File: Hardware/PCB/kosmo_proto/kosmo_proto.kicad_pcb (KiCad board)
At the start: 2 copper layers, 100 x 55 mm, 567 parts, among them J1 Synth_power_2x5, J2 Conn_01x01, J3 Conn_01x01, J4 Conn_01x01, J5 Conn_01x01, J6 Conn_01x01, J7 Conn_01x01

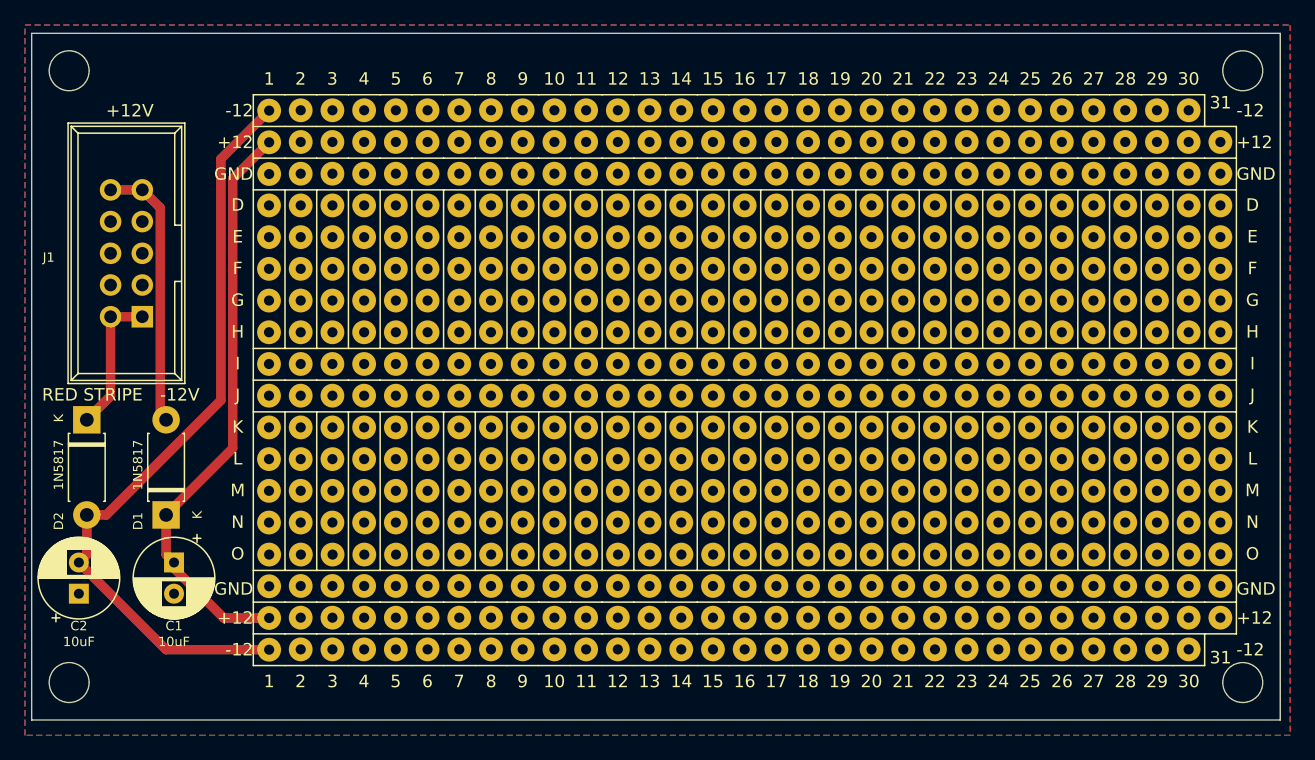
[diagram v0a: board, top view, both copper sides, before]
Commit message: Narrower version with jacks (kosmo_proto_j)
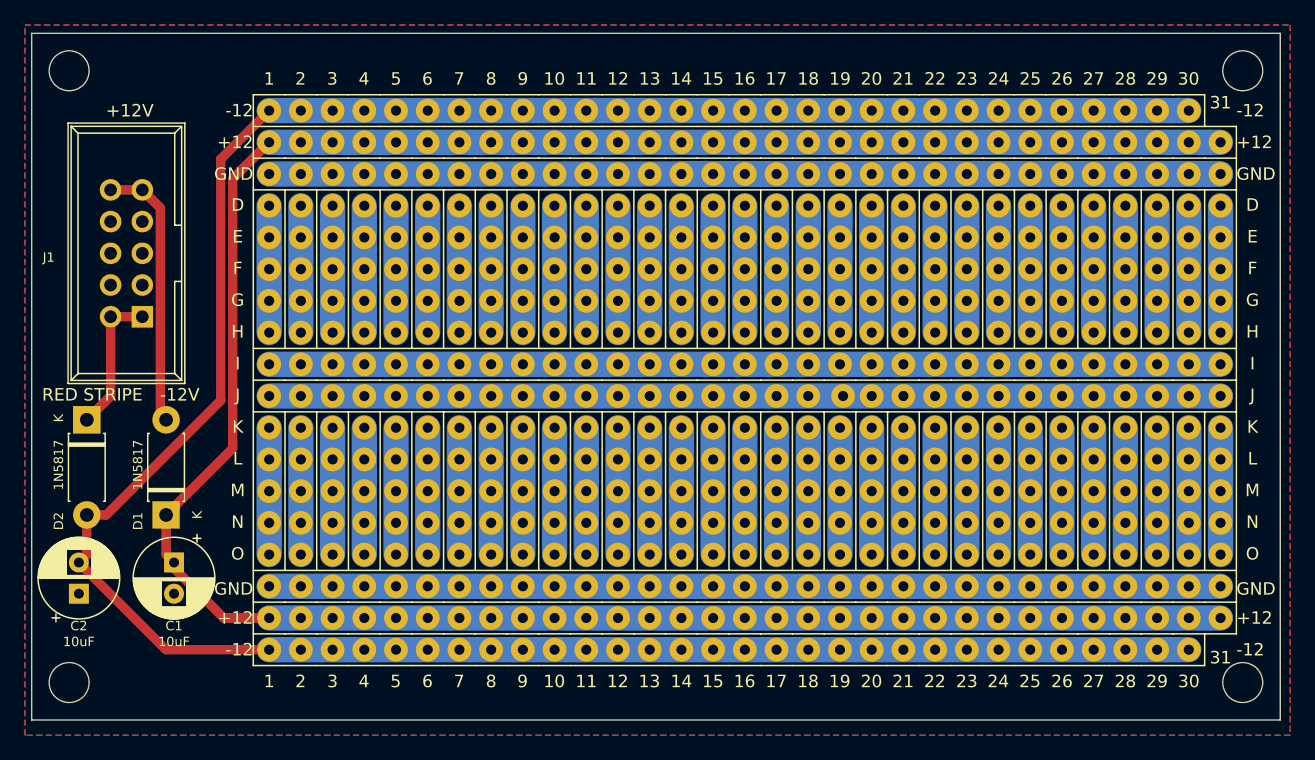
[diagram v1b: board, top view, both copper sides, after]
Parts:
- removed REF** (x4): MountingHole_3.2mm_M3, ao_tht:MountingHole_3.2mm_M3
- removed REF** (x550): PBH, ao_tht:Perf_Board_Hole
- added H1: MountingHole, ao_tht:MountingHole_3.2mm_M3, F.Cu at (48.8, 105.5)
- added H2: MountingHole, ao_tht:MountingHole_3.2mm_M3, F.Cu at (142.8, 105.5)
- added H3: MountingHole, ao_tht:MountingHole_3.2mm_M3, F.Cu at (48.8, 56.5)
- added H4: MountingHole, ao_tht:MountingHole_3.2mm_M3, F.Cu at (142.8, 56.5)
- added J10: 1x1, ao_tht:Perf_Board_Hole, F.Cu at (64.8, 80.0)
- added J100: 1x1, ao_tht:Perf_Board_Hole, F.Cu at (90.2, 80.0)
- added J101: 1x1, ao_tht:Perf_Board_Hole, F.Cu at (92.7, 59.7)
- added J102: 1x1, ao_tht:Perf_Board_Hole, F.Cu at (92.7, 62.2)
- added J103: 1x1, ao_tht:Perf_Board_Hole, F.Cu at (92.7, 64.8)
- added J104: 1x1, ao_tht:Perf_Board_Hole, F.Cu at (92.7, 67.3)
- added J105: 1x1, ao_tht:Perf_Board_Hole, F.Cu at (92.7, 69.8)
- added J106: 1x1, ao_tht:Perf_Board_Hole, F.Cu at (92.7, 72.4)
- added J107: 1x1, ao_tht:Perf_Board_Hole, F.Cu at (92.7, 74.9)
- added J108: 1x1, ao_tht:Perf_Board_Hole, F.Cu at (92.7, 77.5)
- added J109: 1x1, ao_tht:Perf_Board_Hole, F.Cu at (92.7, 80.0)
- added J11: 1x1, ao_tht:Perf_Board_Hole, F.Cu at (67.3, 59.7)
- added J110: 1x1, ao_tht:Perf_Board_Hole, F.Cu at (95.2, 59.7)
- added J111: 1x1, ao_tht:Perf_Board_Hole, F.Cu at (95.2, 62.2)
- added J112: 1x1, ao_tht:Perf_Board_Hole, F.Cu at (95.2, 64.8)
- added J113: 1x1, ao_tht:Perf_Board_Hole, F.Cu at (95.2, 67.3)
- added J114: 1x1, ao_tht:Perf_Board_Hole, F.Cu at (95.2, 69.8)
- added J115: 1x1, ao_tht:Perf_Board_Hole, F.Cu at (95.2, 72.4)
- added J116: 1x1, ao_tht:Perf_Board_Hole, F.Cu at (95.2, 74.9)
- added J117: 1x1, ao_tht:Perf_Board_Hole, F.Cu at (95.2, 77.5)
- added J118: 1x1, ao_tht:Perf_Board_Hole, F.Cu at (95.2, 80.0)
- added J119: 1x1, ao_tht:Perf_Board_Hole, F.Cu at (97.8, 59.7)
- added J12: 1x1, ao_tht:Perf_Board_Hole, F.Cu at (67.3, 62.2)
- added J120: 1x1, ao_tht:Perf_Board_Hole, F.Cu at (97.8, 62.2)
- added J121: 1x1, ao_tht:Perf_Board_Hole, F.Cu at (97.8, 64.8)
- added J122: 1x1, ao_tht:Perf_Board_Hole, F.Cu at (97.8, 67.3)
- added J123: 1x1, ao_tht:Perf_Board_Hole, F.Cu at (97.8, 69.8)
- added J124: 1x1, ao_tht:Perf_Board_Hole, F.Cu at (97.8, 72.4)
- added J125: 1x1, ao_tht:Perf_Board_Hole, F.Cu at (97.8, 74.9)
- added J126: 1x1, ao_tht:Perf_Board_Hole, F.Cu at (97.8, 77.5)
- added J127: 1x1, ao_tht:Perf_Board_Hole, F.Cu at (97.8, 80.0)
- added J128: 1x1, ao_tht:Perf_Board_Hole, F.Cu at (100.3, 59.7)
- added J129: 1x1, ao_tht:Perf_Board_Hole, F.Cu at (100.3, 62.2)
- added J13: 1x1, ao_tht:Perf_Board_Hole, F.Cu at (67.3, 64.8)
- added J130: 1x1, ao_tht:Perf_Board_Hole, F.Cu at (100.3, 64.8)
- added J131: 1x1, ao_tht:Perf_Board_Hole, F.Cu at (100.3, 67.3)
- added J132: 1x1, ao_tht:Perf_Board_Hole, F.Cu at (100.3, 69.8)
- added J133: 1x1, ao_tht:Perf_Board_Hole, F.Cu at (100.3, 72.4)
- added J134: 1x1, ao_tht:Perf_Board_Hole, F.Cu at (100.3, 74.9)
- added J135: 1x1, ao_tht:Perf_Board_Hole, F.Cu at (100.3, 77.5)
- added J136: 1x1, ao_tht:Perf_Board_Hole, F.Cu at (100.3, 80.0)
- added J137: 1x1, ao_tht:Perf_Board_Hole, F.Cu at (102.9, 59.7)
- added J138: 1x1, ao_tht:Perf_Board_Hole, F.Cu at (102.9, 62.2)
- added J139: 1x1, ao_tht:Perf_Board_Hole, F.Cu at (102.9, 64.8)
- added J14: 1x1, ao_tht:Perf_Board_Hole, F.Cu at (67.3, 67.3)
- added J140: 1x1, ao_tht:Perf_Board_Hole, F.Cu at (102.9, 67.3)
- added J141: 1x1, ao_tht:Perf_Board_Hole, F.Cu at (102.9, 69.8)
- added J142: 1x1, ao_tht:Perf_Board_Hole, F.Cu at (102.9, 72.4)
- added J143: 1x1, ao_tht:Perf_Board_Hole, F.Cu at (102.9, 74.9)
- added J144: 1x1, ao_tht:Perf_Board_Hole, F.Cu at (102.9, 77.5)
- added J145: 1x1, ao_tht:Perf_Board_Hole, F.Cu at (102.9, 80.0)
- added J146: 1x1, ao_tht:Perf_Board_Hole, F.Cu at (105.4, 59.7)
- added J147: 1x1, ao_tht:Perf_Board_Hole, F.Cu at (105.4, 62.2)
- added J148: 1x1, ao_tht:Perf_Board_Hole, F.Cu at (105.4, 64.8)
- added J149: 1x1, ao_tht:Perf_Board_Hole, F.Cu at (105.4, 67.3)
- added J15: 1x1, ao_tht:Perf_Board_Hole, F.Cu at (67.3, 69.8)
- added J150: 1x1, ao_tht:Perf_Board_Hole, F.Cu at (105.4, 69.8)
- added J151: 1x1, ao_tht:Perf_Board_Hole, F.Cu at (105.4, 72.4)
- added J152: 1x1, ao_tht:Perf_Board_Hole, F.Cu at (105.4, 74.9)
- added J153: 1x1, ao_tht:Perf_Board_Hole, F.Cu at (105.4, 77.5)
- added J154: 1x1, ao_tht:Perf_Board_Hole, F.Cu at (105.4, 80.0)
- added J155: 1x1, ao_tht:Perf_Board_Hole, F.Cu at (108.0, 59.7)
- added J156: 1x1, ao_tht:Perf_Board_Hole, F.Cu at (108.0, 62.2)
- added J157: 1x1, ao_tht:Perf_Board_Hole, F.Cu at (108.0, 64.8)
- added J158: 1x1, ao_tht:Perf_Board_Hole, F.Cu at (108.0, 67.3)
- added J159: 1x1, ao_tht:Perf_Board_Hole, F.Cu at (108.0, 69.8)
- added J16: 1x1, ao_tht:Perf_Board_Hole, F.Cu at (67.3, 72.4)
- added J160: 1x1, ao_tht:Perf_Board_Hole, F.Cu at (108.0, 72.4)
- added J161: 1x1, ao_tht:Perf_Board_Hole, F.Cu at (108.0, 74.9)
- added J162: 1x1, ao_tht:Perf_Board_Hole, F.Cu at (108.0, 77.5)
- added J163: 1x1, ao_tht:Perf_Board_Hole, F.Cu at (108.0, 80.0)
- added J164: 1x1, ao_tht:Perf_Board_Hole, F.Cu at (110.5, 59.7)
- added J165: 1x1, ao_tht:Perf_Board_Hole, F.Cu at (110.5, 62.2)
- added J166: 1x1, ao_tht:Perf_Board_Hole, F.Cu at (110.5, 64.8)
- added J167: 1x1, ao_tht:Perf_Board_Hole, F.Cu at (110.5, 67.3)
- added J168: 1x1, ao_tht:Perf_Board_Hole, F.Cu at (110.5, 69.8)
- added J169: 1x1, ao_tht:Perf_Board_Hole, F.Cu at (110.5, 72.4)
- added J17: 1x1, ao_tht:Perf_Board_Hole, F.Cu at (67.3, 74.9)
- added J170: 1x1, ao_tht:Perf_Board_Hole, F.Cu at (110.5, 74.9)
- added J171: 1x1, ao_tht:Perf_Board_Hole, F.Cu at (110.5, 77.5)
- added J172: 1x1, ao_tht:Perf_Board_Hole, F.Cu at (110.5, 80.0)
- added J173: 1x1, ao_tht:Perf_Board_Hole, F.Cu at (113.0, 59.7)
- added J174: 1x1, ao_tht:Perf_Board_Hole, F.Cu at (113.0, 62.2)
- added J175: 1x1, ao_tht:Perf_Board_Hole, F.Cu at (113.0, 64.8)
- added J176: 1x1, ao_tht:Perf_Board_Hole, F.Cu at (113.0, 67.3)
- added J177: 1x1, ao_tht:Perf_Board_Hole, F.Cu at (113.0, 69.8)
- added J178: 1x1, ao_tht:Perf_Board_Hole, F.Cu at (113.0, 72.4)
- added J179: 1x1, ao_tht:Perf_Board_Hole, F.Cu at (113.0, 74.9)
- added J18: 1x1, ao_tht:Perf_Board_Hole, F.Cu at (67.3, 77.5)
- added J180: 1x1, ao_tht:Perf_Board_Hole, F.Cu at (113.0, 77.5)
- added J181: 1x1, ao_tht:Perf_Board_Hole, F.Cu at (113.0, 80.0)
- added J182: 1x1, ao_tht:Perf_Board_Hole, F.Cu at (115.6, 59.7)
- added J183: 1x1, ao_tht:Perf_Board_Hole, F.Cu at (115.6, 62.2)
- added J184: 1x1, ao_tht:Perf_Board_Hole, F.Cu at (115.6, 64.8)
- added J185: 1x1, ao_tht:Perf_Board_Hole, F.Cu at (115.6, 67.3)
- added J186: 1x1, ao_tht:Perf_Board_Hole, F.Cu at (115.6, 69.8)
- added J187: 1x1, ao_tht:Perf_Board_Hole, F.Cu at (115.6, 72.4)
- added J188: 1x1, ao_tht:Perf_Board_Hole, F.Cu at (115.6, 74.9)
- added J189: 1x1, ao_tht:Perf_Board_Hole, F.Cu at (115.6, 77.5)
- added J19: 1x1, ao_tht:Perf_Board_Hole, F.Cu at (67.3, 80.0)
- added J190: 1x1, ao_tht:Perf_Board_Hole, F.Cu at (115.6, 80.0)
- added J191: 1x1, ao_tht:Perf_Board_Hole, F.Cu at (118.1, 59.7)
- added J192: 1x1, ao_tht:Perf_Board_Hole, F.Cu at (118.1, 62.2)
- added J193: 1x1, ao_tht:Perf_Board_Hole, F.Cu at (118.1, 64.8)
- added J194: 1x1, ao_tht:Perf_Board_Hole, F.Cu at (118.1, 67.3)
- added J195: 1x1, ao_tht:Perf_Board_Hole, F.Cu at (118.1, 69.8)
- added J196: 1x1, ao_tht:Perf_Board_Hole, F.Cu at (118.1, 72.4)
- added J197: 1x1, ao_tht:Perf_Board_Hole, F.Cu at (118.1, 74.9)
- added J198: 1x1, ao_tht:Perf_Board_Hole, F.Cu at (118.1, 77.5)
- added J199: 1x1, ao_tht:Perf_Board_Hole, F.Cu at (118.1, 80.0)
- added J20: 1x1, ao_tht:Perf_Board_Hole, F.Cu at (69.8, 59.7)
- added J200: 1x1, ao_tht:Perf_Board_Hole, F.Cu at (120.7, 59.7)
- added J201: 1x1, ao_tht:Perf_Board_Hole, F.Cu at (120.7, 62.2)
- added J202: 1x1, ao_tht:Perf_Board_Hole, F.Cu at (120.7, 64.8)
- added J203: 1x1, ao_tht:Perf_Board_Hole, F.Cu at (120.7, 67.3)
- added J204: 1x1, ao_tht:Perf_Board_Hole, F.Cu at (120.7, 69.8)
- added J205: 1x1, ao_tht:Perf_Board_Hole, F.Cu at (120.7, 72.4)
- added J206: 1x1, ao_tht:Perf_Board_Hole, F.Cu at (120.7, 74.9)
- added J207: 1x1, ao_tht:Perf_Board_Hole, F.Cu at (120.7, 77.5)
- added J208: 1x1, ao_tht:Perf_Board_Hole, F.Cu at (120.7, 80.0)
- added J209: 1x1, ao_tht:Perf_Board_Hole, F.Cu at (123.2, 59.7)
- added J21: 1x1, ao_tht:Perf_Board_Hole, F.Cu at (69.8, 62.2)
- added J210: 1x1, ao_tht:Perf_Board_Hole, F.Cu at (123.2, 62.2)
- added J211: 1x1, ao_tht:Perf_Board_Hole, F.Cu at (123.2, 64.8)
- added J212: 1x1, ao_tht:Perf_Board_Hole, F.Cu at (123.2, 67.3)
- added J213: 1x1, ao_tht:Perf_Board_Hole, F.Cu at (123.2, 69.8)
- added J214: 1x1, ao_tht:Perf_Board_Hole, F.Cu at (123.2, 72.4)
- added J215: 1x1, ao_tht:Perf_Board_Hole, F.Cu at (123.2, 74.9)
- added J216: 1x1, ao_tht:Perf_Board_Hole, F.Cu at (123.2, 77.5)
- added J217: 1x1, ao_tht:Perf_Board_Hole, F.Cu at (123.2, 80.0)
- added J218: 1x1, ao_tht:Perf_Board_Hole, F.Cu at (125.7, 59.7)
- added J219: 1x1, ao_tht:Perf_Board_Hole, F.Cu at (125.7, 62.2)
- added J22: 1x1, ao_tht:Perf_Board_Hole, F.Cu at (69.8, 64.8)
- added J220: 1x1, ao_tht:Perf_Board_Hole, F.Cu at (125.7, 64.8)
- added J221: 1x1, ao_tht:Perf_Board_Hole, F.Cu at (125.7, 67.3)
- added J222: 1x1, ao_tht:Perf_Board_Hole, F.Cu at (125.7, 69.8)
- added J223: 1x1, ao_tht:Perf_Board_Hole, F.Cu at (125.7, 72.4)
- added J224: 1x1, ao_tht:Perf_Board_Hole, F.Cu at (125.7, 74.9)
- added J225: 1x1, ao_tht:Perf_Board_Hole, F.Cu at (125.7, 77.5)
- added J226: 1x1, ao_tht:Perf_Board_Hole, F.Cu at (125.7, 80.0)
- added J227: 1x1, ao_tht:Perf_Board_Hole, F.Cu at (128.3, 59.7)
- added J228: 1x1, ao_tht:Perf_Board_Hole, F.Cu at (128.3, 62.2)
- added J229: 1x1, ao_tht:Perf_Board_Hole, F.Cu at (128.3, 64.8)
- added J23: 1x1, ao_tht:Perf_Board_Hole, F.Cu at (69.8, 67.3)
- added J230: 1x1, ao_tht:Perf_Board_Hole, F.Cu at (128.3, 67.3)
- added J231: 1x1, ao_tht:Perf_Board_Hole, F.Cu at (128.3, 69.8)
- added J232: 1x1, ao_tht:Perf_Board_Hole, F.Cu at (128.3, 72.4)
- added J233: 1x1, ao_tht:Perf_Board_Hole, F.Cu at (128.3, 74.9)
- added J234: 1x1, ao_tht:Perf_Board_Hole, F.Cu at (128.3, 77.5)
- added J235: 1x1, ao_tht:Perf_Board_Hole, F.Cu at (128.3, 80.0)
- added J236: 1x1, ao_tht:Perf_Board_Hole, F.Cu at (130.8, 59.7)
- added J237: 1x1, ao_tht:Perf_Board_Hole, F.Cu at (130.8, 62.2)
- added J238: 1x1, ao_tht:Perf_Board_Hole, F.Cu at (130.8, 64.8)
- added J239: 1x1, ao_tht:Perf_Board_Hole, F.Cu at (130.8, 67.3)
- added J24: 1x1, ao_tht:Perf_Board_Hole, F.Cu at (69.8, 69.8)
- added J240: 1x1, ao_tht:Perf_Board_Hole, F.Cu at (130.8, 69.8)
- added J241: 1x1, ao_tht:Perf_Board_Hole, F.Cu at (130.8, 72.4)
- added J242: 1x1, ao_tht:Perf_Board_Hole, F.Cu at (130.8, 74.9)
- added J243: 1x1, ao_tht:Perf_Board_Hole, F.Cu at (130.8, 77.5)
- added J244: 1x1, ao_tht:Perf_Board_Hole, F.Cu at (130.8, 80.0)
- added J245: 1x1, ao_tht:Perf_Board_Hole, F.Cu at (133.3, 59.7)
- added J246: 1x1, ao_tht:Perf_Board_Hole, F.Cu at (133.3, 62.2)
- added J247: 1x1, ao_tht:Perf_Board_Hole, F.Cu at (133.3, 64.8)
- added J248: 1x1, ao_tht:Perf_Board_Hole, F.Cu at (133.3, 67.3)
- added J249: 1x1, ao_tht:Perf_Board_Hole, F.Cu at (133.3, 69.8)
- added J25: 1x1, ao_tht:Perf_Board_Hole, F.Cu at (69.8, 72.4)
- added J250: 1x1, ao_tht:Perf_Board_Hole, F.Cu at (133.3, 72.4)
- added J251: 1x1, ao_tht:Perf_Board_Hole, F.Cu at (133.3, 74.9)
- added J252: 1x1, ao_tht:Perf_Board_Hole, F.Cu at (133.3, 77.5)
- added J253: 1x1, ao_tht:Perf_Board_Hole, F.Cu at (133.3, 80.0)
- added J254: 1x1, ao_tht:Perf_Board_Hole, F.Cu at (135.9, 59.7)
- added J255: 1x1, ao_tht:Perf_Board_Hole, F.Cu at (135.9, 62.2)
- added J256: 1x1, ao_tht:Perf_Board_Hole, F.Cu at (135.9, 64.8)
- added J257: 1x1, ao_tht:Perf_Board_Hole, F.Cu at (135.9, 67.3)
- added J258: 1x1, ao_tht:Perf_Board_Hole, F.Cu at (135.9, 69.8)
- added J259: 1x1, ao_tht:Perf_Board_Hole, F.Cu at (135.9, 72.4)
- added J26: 1x1, ao_tht:Perf_Board_Hole, F.Cu at (69.8, 74.9)
- added J260: 1x1, ao_tht:Perf_Board_Hole, F.Cu at (135.9, 74.9)
- added J261: 1x1, ao_tht:Perf_Board_Hole, F.Cu at (135.9, 77.5)
- added J262: 1x1, ao_tht:Perf_Board_Hole, F.Cu at (135.9, 80.0)
- added J263: 1x1, ao_tht:Perf_Board_Hole, F.Cu at (138.4, 59.7)
- added J264: 1x1, ao_tht:Perf_Board_Hole, F.Cu at (138.4, 62.2)
- added J265: 1x1, ao_tht:Perf_Board_Hole, F.Cu at (138.4, 64.8)
- added J266: 1x1, ao_tht:Perf_Board_Hole, F.Cu at (138.4, 67.3)
- added J267: 1x1, ao_tht:Perf_Board_Hole, F.Cu at (138.4, 69.8)
- added J268: 1x1, ao_tht:Perf_Board_Hole, F.Cu at (138.4, 72.4)
- added J269: 1x1, ao_tht:Perf_Board_Hole, F.Cu at (138.4, 74.9)
- added J27: 1x1, ao_tht:Perf_Board_Hole, F.Cu at (69.8, 77.5)
- added J270: 1x1, ao_tht:Perf_Board_Hole, F.Cu at (138.4, 77.5)
- added J271: 1x1, ao_tht:Perf_Board_Hole, F.Cu at (138.4, 80.0)
- added J273: 1x1, ao_tht:Perf_Board_Hole, F.Cu at (141.0, 62.2)
- added J274: 1x1, ao_tht:Perf_Board_Hole, F.Cu at (141.0, 64.8)
- added J275: 1x1, ao_tht:Perf_Board_Hole, F.Cu at (141.0, 67.3)
- added J276: 1x1, ao_tht:Perf_Board_Hole, F.Cu at (141.0, 69.8)
- added J277: 1x1, ao_tht:Perf_Board_Hole, F.Cu at (141.0, 72.4)
- added J278: 1x1, ao_tht:Perf_Board_Hole, F.Cu at (141.0, 74.9)
- added J279: 1x1, ao_tht:Perf_Board_Hole, F.Cu at (141.0, 77.5)
- added J28: 1x1, ao_tht:Perf_Board_Hole, F.Cu at (69.8, 80.0)
- added J280: 1x1, ao_tht:Perf_Board_Hole, F.Cu at (141.0, 80.0)
- added J281: 1x1, ao_tht:Perf_Board_Hole, F.Cu at (64.8, 82.5)
- added J282: 1x1, ao_tht:Perf_Board_Hole, F.Cu at (64.8, 85.1)
- added J283: 1x1, ao_tht:Perf_Board_Hole, F.Cu at (64.8, 87.6)
- added J284: 1x1, ao_tht:Perf_Board_Hole, F.Cu at (64.8, 90.2)
- added J285: 1x1, ao_tht:Perf_Board_Hole, F.Cu at (64.8, 92.7)
- added J286: 1x1, ao_tht:Perf_Board_Hole, F.Cu at (64.8, 95.2)
- added J287: 1x1, ao_tht:Perf_Board_Hole, F.Cu at (64.8, 97.8)
- added J288: 1x1, ao_tht:Perf_Board_Hole, F.Cu at (64.8, 100.3)
- added J289: 1x1, ao_tht:Perf_Board_Hole, F.Cu at (64.8, 102.9)
- added J29: 1x1, ao_tht:Perf_Board_Hole, F.Cu at (72.4, 59.7)
- added J290: 1x1, ao_tht:Perf_Board_Hole, F.Cu at (67.3, 82.5)
- added J291: 1x1, ao_tht:Perf_Board_Hole, F.Cu at (67.3, 85.1)
- added J292: 1x1, ao_tht:Perf_Board_Hole, F.Cu at (67.3, 87.6)
- added J293: 1x1, ao_tht:Perf_Board_Hole, F.Cu at (67.3, 90.2)
- added J294: 1x1, ao_tht:Perf_Board_Hole, F.Cu at (67.3, 92.7)
- added J295: 1x1, ao_tht:Perf_Board_Hole, F.Cu at (67.3, 95.2)
- added J296: 1x1, ao_tht:Perf_Board_Hole, F.Cu at (67.3, 97.8)
- added J297: 1x1, ao_tht:Perf_Board_Hole, F.Cu at (67.3, 100.3)
- added J298: 1x1, ao_tht:Perf_Board_Hole, F.Cu at (67.3, 102.9)
- added J299: 1x1, ao_tht:Perf_Board_Hole, F.Cu at (69.8, 82.5)
- added J30: 1x1, ao_tht:Perf_Board_Hole, F.Cu at (72.4, 62.2)
- added J300: 1x1, ao_tht:Perf_Board_Hole, F.Cu at (69.8, 85.1)
- added J301: 1x1, ao_tht:Perf_Board_Hole, F.Cu at (69.8, 87.6)
- added J302: 1x1, ao_tht:Perf_Board_Hole, F.Cu at (69.8, 90.2)
- added J303: 1x1, ao_tht:Perf_Board_Hole, F.Cu at (69.8, 92.7)
- added J304: 1x1, ao_tht:Perf_Board_Hole, F.Cu at (69.8, 95.2)
- added J305: 1x1, ao_tht:Perf_Board_Hole, F.Cu at (69.8, 97.8)
- added J306: 1x1, ao_tht:Perf_Board_Hole, F.Cu at (69.8, 100.3)
- added J307: 1x1, ao_tht:Perf_Board_Hole, F.Cu at (69.8, 102.9)
- added J308: 1x1, ao_tht:Perf_Board_Hole, F.Cu at (72.4, 82.5)
- added J309: 1x1, ao_tht:Perf_Board_Hole, F.Cu at (72.4, 85.1)
- added J31: 1x1, ao_tht:Perf_Board_Hole, F.Cu at (72.4, 64.8)
- added J310: 1x1, ao_tht:Perf_Board_Hole, F.Cu at (72.4, 87.6)
- added J311: 1x1, ao_tht:Perf_Board_Hole, F.Cu at (72.4, 90.2)
- added J312: 1x1, ao_tht:Perf_Board_Hole, F.Cu at (72.4, 92.7)
- added J313: 1x1, ao_tht:Perf_Board_Hole, F.Cu at (72.4, 95.2)
- added J314: 1x1, ao_tht:Perf_Board_Hole, F.Cu at (72.4, 97.8)
- added J315: 1x1, ao_tht:Perf_Board_Hole, F.Cu at (72.4, 100.3)
- added J316: 1x1, ao_tht:Perf_Board_Hole, F.Cu at (72.4, 102.9)
- added J317: 1x1, ao_tht:Perf_Board_Hole, F.Cu at (74.9, 82.5)
- added J318: 1x1, ao_tht:Perf_Board_Hole, F.Cu at (74.9, 85.1)
- added J319: 1x1, ao_tht:Perf_Board_Hole, F.Cu at (74.9, 87.6)
- added J32: 1x1, ao_tht:Perf_Board_Hole, F.Cu at (72.4, 67.3)
- added J320: 1x1, ao_tht:Perf_Board_Hole, F.Cu at (74.9, 90.2)
- added J321: 1x1, ao_tht:Perf_Board_Hole, F.Cu at (74.9, 92.7)
- added J322: 1x1, ao_tht:Perf_Board_Hole, F.Cu at (74.9, 95.2)
- added J323: 1x1, ao_tht:Perf_Board_Hole, F.Cu at (74.9, 97.8)
- added J324: 1x1, ao_tht:Perf_Board_Hole, F.Cu at (74.9, 100.3)
- added J325: 1x1, ao_tht:Perf_Board_Hole, F.Cu at (74.9, 102.9)
- added J326: 1x1, ao_tht:Perf_Board_Hole, F.Cu at (77.5, 82.5)
- added J327: 1x1, ao_tht:Perf_Board_Hole, F.Cu at (77.5, 85.1)
- added J328: 1x1, ao_tht:Perf_Board_Hole, F.Cu at (77.5, 87.6)
- added J329: 1x1, ao_tht:Perf_Board_Hole, F.Cu at (77.5, 90.2)
- added J33: 1x1, ao_tht:Perf_Board_Hole, F.Cu at (72.4, 69.8)
- added J330: 1x1, ao_tht:Perf_Board_Hole, F.Cu at (77.5, 92.7)
- added J331: 1x1, ao_tht:Perf_Board_Hole, F.Cu at (77.5, 95.2)
- added J332: 1x1, ao_tht:Perf_Board_Hole, F.Cu at (77.5, 97.8)
- added J333: 1x1, ao_tht:Perf_Board_Hole, F.Cu at (77.5, 100.3)
- added J334: 1x1, ao_tht:Perf_Board_Hole, F.Cu at (77.5, 102.9)
- added J335: 1x1, ao_tht:Perf_Board_Hole, F.Cu at (80.0, 82.5)
- added J336: 1x1, ao_tht:Perf_Board_Hole, F.Cu at (80.0, 85.1)
- added J337: 1x1, ao_tht:Perf_Board_Hole, F.Cu at (80.0, 87.6)
- added J338: 1x1, ao_tht:Perf_Board_Hole, F.Cu at (80.0, 90.2)
- added J339: 1x1, ao_tht:Perf_Board_Hole, F.Cu at (80.0, 92.7)
- added J34: 1x1, ao_tht:Perf_Board_Hole, F.Cu at (72.4, 72.4)
- added J340: 1x1, ao_tht:Perf_Board_Hole, F.Cu at (80.0, 95.2)
- added J341: 1x1, ao_tht:Perf_Board_Hole, F.Cu at (80.0, 97.8)
- added J342: 1x1, ao_tht:Perf_Board_Hole, F.Cu at (80.0, 100.3)
- added J343: 1x1, ao_tht:Perf_Board_Hole, F.Cu at (80.0, 102.9)
- added J344: 1x1, ao_tht:Perf_Board_Hole, F.Cu at (82.5, 82.5)
- added J345: 1x1, ao_tht:Perf_Board_Hole, F.Cu at (82.5, 85.1)
- added J346: 1x1, ao_tht:Perf_Board_Hole, F.Cu at (82.5, 87.6)
- added J347: 1x1, ao_tht:Perf_Board_Hole, F.Cu at (82.5, 90.2)
- added J348: 1x1, ao_tht:Perf_Board_Hole, F.Cu at (82.5, 92.7)
- added J349: 1x1, ao_tht:Perf_Board_Hole, F.Cu at (82.5, 95.2)
- added J35: 1x1, ao_tht:Perf_Board_Hole, F.Cu at (72.4, 74.9)
- added J350: 1x1, ao_tht:Perf_Board_Hole, F.Cu at (82.5, 97.8)
- added J351: 1x1, ao_tht:Perf_Board_Hole, F.Cu at (82.5, 100.3)
- added J352: 1x1, ao_tht:Perf_Board_Hole, F.Cu at (82.5, 102.9)
- added J353: 1x1, ao_tht:Perf_Board_Hole, F.Cu at (85.1, 82.5)
- added J354: 1x1, ao_tht:Perf_Board_Hole, F.Cu at (85.1, 85.1)
- added J355: 1x1, ao_tht:Perf_Board_Hole, F.Cu at (85.1, 87.6)
- added J356: 1x1, ao_tht:Perf_Board_Hole, F.Cu at (85.1, 90.2)
- added J357: 1x1, ao_tht:Perf_Board_Hole, F.Cu at (85.1, 92.7)
- added J358: 1x1, ao_tht:Perf_Board_Hole, F.Cu at (85.1, 95.2)
- added J359: 1x1, ao_tht:Perf_Board_Hole, F.Cu at (85.1, 97.8)
- added J36: 1x1, ao_tht:Perf_Board_Hole, F.Cu at (72.4, 77.5)
- added J360: 1x1, ao_tht:Perf_Board_Hole, F.Cu at (85.1, 100.3)
- added J361: 1x1, ao_tht:Perf_Board_Hole, F.Cu at (85.1, 102.9)
- added J362: 1x1, ao_tht:Perf_Board_Hole, F.Cu at (87.6, 82.5)
- added J363: 1x1, ao_tht:Perf_Board_Hole, F.Cu at (87.6, 85.1)
- added J364: 1x1, ao_tht:Perf_Board_Hole, F.Cu at (87.6, 87.6)
- added J365: 1x1, ao_tht:Perf_Board_Hole, F.Cu at (87.6, 90.2)
- added J366: 1x1, ao_tht:Perf_Board_Hole, F.Cu at (87.6, 92.7)
- added J367: 1x1, ao_tht:Perf_Board_Hole, F.Cu at (87.6, 95.2)
- added J368: 1x1, ao_tht:Perf_Board_Hole, F.Cu at (87.6, 97.8)
- added J369: 1x1, ao_tht:Perf_Board_Hole, F.Cu at (87.6, 100.3)
- added J37: 1x1, ao_tht:Perf_Board_Hole, F.Cu at (72.4, 80.0)
- added J370: 1x1, ao_tht:Perf_Board_Hole, F.Cu at (87.6, 102.9)
- added J371: 1x1, ao_tht:Perf_Board_Hole, F.Cu at (90.2, 82.5)
- added J372: 1x1, ao_tht:Perf_Board_Hole, F.Cu at (90.2, 85.1)
- added J373: 1x1, ao_tht:Perf_Board_Hole, F.Cu at (90.2, 87.6)
- added J374: 1x1, ao_tht:Perf_Board_Hole, F.Cu at (90.2, 90.2)
- added J375: 1x1, ao_tht:Perf_Board_Hole, F.Cu at (90.2, 92.7)
- added J376: 1x1, ao_tht:Perf_Board_Hole, F.Cu at (90.2, 95.2)
- added J377: 1x1, ao_tht:Perf_Board_Hole, F.Cu at (90.2, 97.8)
- added J378: 1x1, ao_tht:Perf_Board_Hole, F.Cu at (90.2, 100.3)
- added J379: 1x1, ao_tht:Perf_Board_Hole, F.Cu at (90.2, 102.9)
- added J38: 1x1, ao_tht:Perf_Board_Hole, F.Cu at (74.9, 59.7)
- added J380: 1x1, ao_tht:Perf_Board_Hole, F.Cu at (92.7, 82.5)
- added J381: 1x1, ao_tht:Perf_Board_Hole, F.Cu at (92.7, 85.1)
- added J382: 1x1, ao_tht:Perf_Board_Hole, F.Cu at (92.7, 87.6)
- added J383: 1x1, ao_tht:Perf_Board_Hole, F.Cu at (92.7, 90.2)
- added J384: 1x1, ao_tht:Perf_Board_Hole, F.Cu at (92.7, 92.7)
- added J385: 1x1, ao_tht:Perf_Board_Hole, F.Cu at (92.7, 95.2)
- added J386: 1x1, ao_tht:Perf_Board_Hole, F.Cu at (92.7, 97.8)
- added J387: 1x1, ao_tht:Perf_Board_Hole, F.Cu at (92.7, 100.3)
- added J388: 1x1, ao_tht:Perf_Board_Hole, F.Cu at (92.7, 102.9)
- added J389: 1x1, ao_tht:Perf_Board_Hole, F.Cu at (95.2, 82.5)
- added J39: 1x1, ao_tht:Perf_Board_Hole, F.Cu at (74.9, 62.2)
- added J390: 1x1, ao_tht:Perf_Board_Hole, F.Cu at (95.2, 85.1)
- added J391: 1x1, ao_tht:Perf_Board_Hole, F.Cu at (95.2, 87.6)
- added J392: 1x1, ao_tht:Perf_Board_Hole, F.Cu at (95.2, 90.2)
- added J393: 1x1, ao_tht:Perf_Board_Hole, F.Cu at (95.2, 92.7)
- added J394: 1x1, ao_tht:Perf_Board_Hole, F.Cu at (95.2, 95.2)
- added J395: 1x1, ao_tht:Perf_Board_Hole, F.Cu at (95.2, 97.8)
- added J396: 1x1, ao_tht:Perf_Board_Hole, F.Cu at (95.2, 100.3)
- added J397: 1x1, ao_tht:Perf_Board_Hole, F.Cu at (95.2, 102.9)
- added J398: 1x1, ao_tht:Perf_Board_Hole, F.Cu at (97.8, 82.5)
- added J399: 1x1, ao_tht:Perf_Board_Hole, F.Cu at (97.8, 85.1)
- added J40: 1x1, ao_tht:Perf_Board_Hole, F.Cu at (74.9, 64.8)
- added J400: 1x1, ao_tht:Perf_Board_Hole, F.Cu at (97.8, 87.6)
- added J401: 1x1, ao_tht:Perf_Board_Hole, F.Cu at (97.8, 90.2)
- added J402: 1x1, ao_tht:Perf_Board_Hole, F.Cu at (97.8, 92.7)
- added J403: 1x1, ao_tht:Perf_Board_Hole, F.Cu at (97.8, 95.2)
- added J404: 1x1, ao_tht:Perf_Board_Hole, F.Cu at (97.8, 97.8)
- added J405: 1x1, ao_tht:Perf_Board_Hole, F.Cu at (97.8, 100.3)
- added J406: 1x1, ao_tht:Perf_Board_Hole, F.Cu at (97.8, 102.9)
- added J407: 1x1, ao_tht:Perf_Board_Hole, F.Cu at (100.3, 82.5)
- added J408: 1x1, ao_tht:Perf_Board_Hole, F.Cu at (100.3, 85.1)
- added J409: 1x1, ao_tht:Perf_Board_Hole, F.Cu at (100.3, 87.6)
- added J41: 1x1, ao_tht:Perf_Board_Hole, F.Cu at (74.9, 67.3)
- added J410: 1x1, ao_tht:Perf_Board_Hole, F.Cu at (100.3, 90.2)
- added J411: 1x1, ao_tht:Perf_Board_Hole, F.Cu at (100.3, 92.7)
- added J412: 1x1, ao_tht:Perf_Board_Hole, F.Cu at (100.3, 95.2)
- added J413: 1x1, ao_tht:Perf_Board_Hole, F.Cu at (100.3, 97.8)
- added J414: 1x1, ao_tht:Perf_Board_Hole, F.Cu at (100.3, 100.3)
- added J415: 1x1, ao_tht:Perf_Board_Hole, F.Cu at (100.3, 102.9)
- added J416: 1x1, ao_tht:Perf_Board_Hole, F.Cu at (102.9, 82.5)
- added J417: 1x1, ao_tht:Perf_Board_Hole, F.Cu at (102.9, 85.1)
- added J418: 1x1, ao_tht:Perf_Board_Hole, F.Cu at (102.9, 87.6)
- added J419: 1x1, ao_tht:Perf_Board_Hole, F.Cu at (102.9, 90.2)
- added J42: 1x1, ao_tht:Perf_Board_Hole, F.Cu at (74.9, 69.8)
- added J420: 1x1, ao_tht:Perf_Board_Hole, F.Cu at (102.9, 92.7)
- added J421: 1x1, ao_tht:Perf_Board_Hole, F.Cu at (102.9, 95.2)
- added J422: 1x1, ao_tht:Perf_Board_Hole, F.Cu at (102.9, 97.8)
- added J423: 1x1, ao_tht:Perf_Board_Hole, F.Cu at (102.9, 100.3)
- added J424: 1x1, ao_tht:Perf_Board_Hole, F.Cu at (102.9, 102.9)
- added J425: 1x1, ao_tht:Perf_Board_Hole, F.Cu at (105.4, 82.5)
- added J426: 1x1, ao_tht:Perf_Board_Hole, F.Cu at (105.4, 85.1)
- added J427: 1x1, ao_tht:Perf_Board_Hole, F.Cu at (105.4, 87.6)
- added J428: 1x1, ao_tht:Perf_Board_Hole, F.Cu at (105.4, 90.2)
- added J429: 1x1, ao_tht:Perf_Board_Hole, F.Cu at (105.4, 92.7)
- added J43: 1x1, ao_tht:Perf_Board_Hole, F.Cu at (74.9, 72.4)
- added J430: 1x1, ao_tht:Perf_Board_Hole, F.Cu at (105.4, 95.2)
- added J431: 1x1, ao_tht:Perf_Board_Hole, F.Cu at (105.4, 97.8)
- added J432: 1x1, ao_tht:Perf_Board_Hole, F.Cu at (105.4, 100.3)
- added J433: 1x1, ao_tht:Perf_Board_Hole, F.Cu at (105.4, 102.9)
- added J434: 1x1, ao_tht:Perf_Board_Hole, F.Cu at (108.0, 82.5)
- added J435: 1x1, ao_tht:Perf_Board_Hole, F.Cu at (108.0, 85.1)
- added J436: 1x1, ao_tht:Perf_Board_Hole, F.Cu at (108.0, 87.6)
- added J437: 1x1, ao_tht:Perf_Board_Hole, F.Cu at (108.0, 90.2)
- added J438: 1x1, ao_tht:Perf_Board_Hole, F.Cu at (108.0, 92.7)
- added J439: 1x1, ao_tht:Perf_Board_Hole, F.Cu at (108.0, 95.2)
- added J44: 1x1, ao_tht:Perf_Board_Hole, F.Cu at (74.9, 74.9)
- added J440: 1x1, ao_tht:Perf_Board_Hole, F.Cu at (108.0, 97.8)
- added J441: 1x1, ao_tht:Perf_Board_Hole, F.Cu at (108.0, 100.3)
- added J442: 1x1, ao_tht:Perf_Board_Hole, F.Cu at (108.0, 102.9)
- added J443: 1x1, ao_tht:Perf_Board_Hole, F.Cu at (110.7, 82.5)
- added J444: 1x1, ao_tht:Perf_Board_Hole, F.Cu at (110.5, 85.1)
- added J445: 1x1, ao_tht:Perf_Board_Hole, F.Cu at (110.5, 87.6)
- added J446: 1x1, ao_tht:Perf_Board_Hole, F.Cu at (110.5, 90.2)
- added J447: 1x1, ao_tht:Perf_Board_Hole, F.Cu at (110.5, 92.7)
- added J448: 1x1, ao_tht:Perf_Board_Hole, F.Cu at (110.5, 95.2)
- added J449: 1x1, ao_tht:Perf_Board_Hole, F.Cu at (110.5, 97.8)
- added J45: 1x1, ao_tht:Perf_Board_Hole, F.Cu at (74.9, 77.5)
- added J450: 1x1, ao_tht:Perf_Board_Hole, F.Cu at (110.5, 100.3)
- added J451: 1x1, ao_tht:Perf_Board_Hole, F.Cu at (110.5, 102.9)
- added J452: 1x1, ao_tht:Perf_Board_Hole, F.Cu at (113.0, 82.5)
- added J453: 1x1, ao_tht:Perf_Board_Hole, F.Cu at (113.0, 85.1)
- added J454: 1x1, ao_tht:Perf_Board_Hole, F.Cu at (113.0, 87.6)
- added J455: 1x1, ao_tht:Perf_Board_Hole, F.Cu at (113.0, 90.2)
- added J456: 1x1, ao_tht:Perf_Board_Hole, F.Cu at (113.0, 92.7)
- added J457: 1x1, ao_tht:Perf_Board_Hole, F.Cu at (113.0, 95.2)
- added J458: 1x1, ao_tht:Perf_Board_Hole, F.Cu at (113.0, 97.8)
- added J459: 1x1, ao_tht:Perf_Board_Hole, F.Cu at (113.0, 100.3)
- added J46: 1x1, ao_tht:Perf_Board_Hole, F.Cu at (74.9, 80.0)
- added J460: 1x1, ao_tht:Perf_Board_Hole, F.Cu at (113.0, 102.9)
- added J461: 1x1, ao_tht:Perf_Board_Hole, F.Cu at (115.6, 82.5)
- added J462: 1x1, ao_tht:Perf_Board_Hole, F.Cu at (115.6, 85.1)
- added J463: 1x1, ao_tht:Perf_Board_Hole, F.Cu at (115.6, 87.6)
- added J464: 1x1, ao_tht:Perf_Board_Hole, F.Cu at (115.6, 90.2)
- added J465: 1x1, ao_tht:Perf_Board_Hole, F.Cu at (115.6, 92.7)
- added J466: 1x1, ao_tht:Perf_Board_Hole, F.Cu at (115.6, 95.2)
- added J467: 1x1, ao_tht:Perf_Board_Hole, F.Cu at (115.6, 97.8)
- added J468: 1x1, ao_tht:Perf_Board_Hole, F.Cu at (115.6, 100.3)
- added J469: 1x1, ao_tht:Perf_Board_Hole, F.Cu at (115.6, 102.9)
- added J47: 1x1, ao_tht:Perf_Board_Hole, F.Cu at (77.5, 59.7)
- added J470: 1x1, ao_tht:Perf_Board_Hole, F.Cu at (118.1, 82.5)
- added J471: 1x1, ao_tht:Perf_Board_Hole, F.Cu at (118.1, 85.1)
- added J472: 1x1, ao_tht:Perf_Board_Hole, F.Cu at (118.1, 87.6)
- added J473: 1x1, ao_tht:Perf_Board_Hole, F.Cu at (118.1, 90.2)
- added J474: 1x1, ao_tht:Perf_Board_Hole, F.Cu at (118.1, 92.7)
- added J475: 1x1, ao_tht:Perf_Board_Hole, F.Cu at (118.1, 95.2)
- added J476: 1x1, ao_tht:Perf_Board_Hole, F.Cu at (118.1, 97.8)
- added J477: 1x1, ao_tht:Perf_Board_Hole, F.Cu at (118.1, 100.3)
- added J478: 1x1, ao_tht:Perf_Board_Hole, F.Cu at (118.1, 102.9)
- added J479: 1x1, ao_tht:Perf_Board_Hole, F.Cu at (120.7, 82.5)
- added J48: 1x1, ao_tht:Perf_Board_Hole, F.Cu at (77.5, 62.2)
- added J480: 1x1, ao_tht:Perf_Board_Hole, F.Cu at (120.7, 85.1)
- added J481: 1x1, ao_tht:Perf_Board_Hole, F.Cu at (120.7, 87.6)
- added J482: 1x1, ao_tht:Perf_Board_Hole, F.Cu at (120.7, 90.2)
- added J483: 1x1, ao_tht:Perf_Board_Hole, F.Cu at (120.7, 92.7)
- added J484: 1x1, ao_tht:Perf_Board_Hole, F.Cu at (120.7, 95.2)
- added J485: 1x1, ao_tht:Perf_Board_Hole, F.Cu at (120.7, 97.8)
- added J486: 1x1, ao_tht:Perf_Board_Hole, F.Cu at (120.7, 100.3)
- added J487: 1x1, ao_tht:Perf_Board_Hole, F.Cu at (120.7, 102.9)
- added J488: 1x1, ao_tht:Perf_Board_Hole, F.Cu at (123.2, 82.5)
- added J489: 1x1, ao_tht:Perf_Board_Hole, F.Cu at (123.2, 85.1)
- added J49: 1x1, ao_tht:Perf_Board_Hole, F.Cu at (77.5, 64.8)
- added J490: 1x1, ao_tht:Perf_Board_Hole, F.Cu at (123.2, 87.6)
- added J491: 1x1, ao_tht:Perf_Board_Hole, F.Cu at (123.2, 90.2)
- added J492: 1x1, ao_tht:Perf_Board_Hole, F.Cu at (123.2, 92.7)
- added J493: 1x1, ao_tht:Perf_Board_Hole, F.Cu at (123.2, 95.2)
- added J494: 1x1, ao_tht:Perf_Board_Hole, F.Cu at (123.2, 97.8)
- added J495: 1x1, ao_tht:Perf_Board_Hole, F.Cu at (123.2, 100.3)
- added J496: 1x1, ao_tht:Perf_Board_Hole, F.Cu at (123.2, 102.9)
- added J497: 1x1, ao_tht:Perf_Board_Hole, F.Cu at (125.7, 82.5)
- added J498: 1x1, ao_tht:Perf_Board_Hole, F.Cu at (125.7, 85.1)
- added J499: 1x1, ao_tht:Perf_Board_Hole, F.Cu at (125.7, 87.6)
- added J50: 1x1, ao_tht:Perf_Board_Hole, F.Cu at (77.5, 67.3)
- added J500: 1x1, ao_tht:Perf_Board_Hole, F.Cu at (125.7, 90.2)
- added J501: 1x1, ao_tht:Perf_Board_Hole, F.Cu at (125.7, 92.7)
- added J502: 1x1, ao_tht:Perf_Board_Hole, F.Cu at (125.7, 95.2)
- added J503: 1x1, ao_tht:Perf_Board_Hole, F.Cu at (125.7, 97.8)
- added J504: 1x1, ao_tht:Perf_Board_Hole, F.Cu at (125.7, 100.3)
- added J505: 1x1, ao_tht:Perf_Board_Hole, F.Cu at (125.7, 102.9)
- added J506: 1x1, ao_tht:Perf_Board_Hole, F.Cu at (128.3, 82.5)
- added J507: 1x1, ao_tht:Perf_Board_Hole, F.Cu at (128.3, 85.1)
- added J508: 1x1, ao_tht:Perf_Board_Hole, F.Cu at (128.3, 87.6)
- added J509: 1x1, ao_tht:Perf_Board_Hole, F.Cu at (128.3, 90.2)
- added J51: 1x1, ao_tht:Perf_Board_Hole, F.Cu at (77.5, 69.8)
- added J510: 1x1, ao_tht:Perf_Board_Hole, F.Cu at (128.3, 92.7)
- added J511: 1x1, ao_tht:Perf_Board_Hole, F.Cu at (128.3, 95.2)
- added J512: 1x1, ao_tht:Perf_Board_Hole, F.Cu at (128.3, 97.8)
- added J513: 1x1, ao_tht:Perf_Board_Hole, F.Cu at (128.3, 100.3)
- added J514: 1x1, ao_tht:Perf_Board_Hole, F.Cu at (128.3, 102.9)
- added J515: 1x1, ao_tht:Perf_Board_Hole, F.Cu at (130.8, 82.5)
- added J516: 1x1, ao_tht:Perf_Board_Hole, F.Cu at (130.8, 85.1)
- added J517: 1x1, ao_tht:Perf_Board_Hole, F.Cu at (130.8, 87.6)
- added J518: 1x1, ao_tht:Perf_Board_Hole, F.Cu at (130.8, 90.2)
- added J519: 1x1, ao_tht:Perf_Board_Hole, F.Cu at (130.8, 92.7)
- added J52: 1x1, ao_tht:Perf_Board_Hole, F.Cu at (77.5, 72.4)
- added J520: 1x1, ao_tht:Perf_Board_Hole, F.Cu at (130.8, 95.2)
- added J521: 1x1, ao_tht:Perf_Board_Hole, F.Cu at (130.8, 97.8)
- added J522: 1x1, ao_tht:Perf_Board_Hole, F.Cu at (130.8, 100.3)
- added J523: 1x1, ao_tht:Perf_Board_Hole, F.Cu at (130.8, 102.9)
- added J524: 1x1, ao_tht:Perf_Board_Hole, F.Cu at (133.3, 82.5)
- added J525: 1x1, ao_tht:Perf_Board_Hole, F.Cu at (133.3, 85.1)
- added J526: 1x1, ao_tht:Perf_Board_Hole, F.Cu at (133.3, 87.6)
- added J527: 1x1, ao_tht:Perf_Board_Hole, F.Cu at (133.3, 90.2)
- added J528: 1x1, ao_tht:Perf_Board_Hole, F.Cu at (133.3, 92.7)
- added J529: 1x1, ao_tht:Perf_Board_Hole, F.Cu at (133.3, 95.2)
- added J53: 1x1, ao_tht:Perf_Board_Hole, F.Cu at (77.5, 74.9)
- added J530: 1x1, ao_tht:Perf_Board_Hole, F.Cu at (133.3, 97.8)
- added J531: 1x1, ao_tht:Perf_Board_Hole, F.Cu at (133.3, 100.3)
- added J532: 1x1, ao_tht:Perf_Board_Hole, F.Cu at (133.3, 102.9)
- added J533: 1x1, ao_tht:Perf_Board_Hole, F.Cu at (135.9, 82.5)
- added J534: 1x1, ao_tht:Perf_Board_Hole, F.Cu at (135.9, 85.1)
- added J535: 1x1, ao_tht:Perf_Board_Hole, F.Cu at (135.9, 87.6)
- added J536: 1x1, ao_tht:Perf_Board_Hole, F.Cu at (135.9, 90.2)
- added J537: 1x1, ao_tht:Perf_Board_Hole, F.Cu at (135.9, 92.7)
- added J538: 1x1, ao_tht:Perf_Board_Hole, F.Cu at (135.9, 95.2)
- added J539: 1x1, ao_tht:Perf_Board_Hole, F.Cu at (135.9, 97.8)
- added J54: 1x1, ao_tht:Perf_Board_Hole, F.Cu at (77.5, 77.5)
- added J540: 1x1, ao_tht:Perf_Board_Hole, F.Cu at (135.9, 100.3)
- added J541: 1x1, ao_tht:Perf_Board_Hole, F.Cu at (135.9, 102.9)
- added J542: 1x1, ao_tht:Perf_Board_Hole, F.Cu at (138.4, 82.5)
- added J543: 1x1, ao_tht:Perf_Board_Hole, F.Cu at (138.4, 85.1)
- added J544: 1x1, ao_tht:Perf_Board_Hole, F.Cu at (138.4, 87.6)
- added J545: 1x1, ao_tht:Perf_Board_Hole, F.Cu at (138.4, 90.2)
- added J546: 1x1, ao_tht:Perf_Board_Hole, F.Cu at (138.4, 92.7)
- added J547: 1x1, ao_tht:Perf_Board_Hole, F.Cu at (138.4, 95.2)
- added J548: 1x1, ao_tht:Perf_Board_Hole, F.Cu at (138.4, 97.8)
- added J549: 1x1, ao_tht:Perf_Board_Hole, F.Cu at (138.4, 100.3)
- added J55: 1x1, ao_tht:Perf_Board_Hole, F.Cu at (77.5, 80.0)
- added J550: 1x1, ao_tht:Perf_Board_Hole, F.Cu at (138.4, 102.9)
- added J551: 1x1, ao_tht:Perf_Board_Hole, F.Cu at (141.0, 82.5)
- added J552: 1x1, ao_tht:Perf_Board_Hole, F.Cu at (141.0, 85.1)
- added J553: 1x1, ao_tht:Perf_Board_Hole, F.Cu at (141.0, 87.6)
- added J554: 1x1, ao_tht:Perf_Board_Hole, F.Cu at (141.0, 90.2)
- added J555: 1x1, ao_tht:Perf_Board_Hole, F.Cu at (141.0, 92.7)
- added J556: 1x1, ao_tht:Perf_Board_Hole, F.Cu at (141.0, 95.2)
- added J557: 1x1, ao_tht:Perf_Board_Hole, F.Cu at (141.0, 97.8)
- added J558: 1x1, ao_tht:Perf_Board_Hole, F.Cu at (141.0, 100.3)
- added J56: 1x1, ao_tht:Perf_Board_Hole, F.Cu at (80.0, 59.7)
- added J57: 1x1, ao_tht:Perf_Board_Hole, F.Cu at (80.0, 62.2)
- added J58: 1x1, ao_tht:Perf_Board_Hole, F.Cu at (80.0, 64.8)
- added J59: 1x1, ao_tht:Perf_Board_Hole, F.Cu at (80.0, 67.3)
- added J60: 1x1, ao_tht:Perf_Board_Hole, F.Cu at (80.0, 69.8)
- added J61: 1x1, ao_tht:Perf_Board_Hole, F.Cu at (80.0, 72.4)
- added J62: 1x1, ao_tht:Perf_Board_Hole, F.Cu at (80.0, 74.9)
- added J63: 1x1, ao_tht:Perf_Board_Hole, F.Cu at (80.0, 77.5)
- added J64: 1x1, ao_tht:Perf_Board_Hole, F.Cu at (80.0, 80.0)
- added J65: 1x1, ao_tht:Perf_Board_Hole, F.Cu at (82.5, 59.7)
- added J66: 1x1, ao_tht:Perf_Board_Hole, F.Cu at (82.5, 62.2)
- added J67: 1x1, ao_tht:Perf_Board_Hole, F.Cu at (82.5, 64.8)
- added J68: 1x1, ao_tht:Perf_Board_Hole, F.Cu at (82.5, 67.3)
- added J69: 1x1, ao_tht:Perf_Board_Hole, F.Cu at (82.5, 69.8)
- added J70: 1x1, ao_tht:Perf_Board_Hole, F.Cu at (82.5, 72.4)
- added J71: 1x1, ao_tht:Perf_Board_Hole, F.Cu at (82.5, 74.9)
- added J72: 1x1, ao_tht:Perf_Board_Hole, F.Cu at (82.5, 77.5)
- added J73: 1x1, ao_tht:Perf_Board_Hole, F.Cu at (82.5, 80.0)
- added J74: 1x1, ao_tht:Perf_Board_Hole, F.Cu at (85.1, 59.7)
- added J75: 1x1, ao_tht:Perf_Board_Hole, F.Cu at (85.1, 62.2)
- added J76: 1x1, ao_tht:Perf_Board_Hole, F.Cu at (85.1, 64.8)
- added J77: 1x1, ao_tht:Perf_Board_Hole, F.Cu at (85.1, 67.3)
- added J78: 1x1, ao_tht:Perf_Board_Hole, F.Cu at (85.1, 69.8)
- added J79: 1x1, ao_tht:Perf_Board_Hole, F.Cu at (85.1, 72.4)
- added J8: 1x1, ao_tht:Perf_Board_Hole, F.Cu at (64.8, 74.9)
- added J80: 1x1, ao_tht:Perf_Board_Hole, F.Cu at (85.1, 74.9)
- added J81: 1x1, ao_tht:Perf_Board_Hole, F.Cu at (85.1, 77.5)
- added J82: 1x1, ao_tht:Perf_Board_Hole, F.Cu at (85.1, 80.0)
- added J83: 1x1, ao_tht:Perf_Board_Hole, F.Cu at (87.6, 59.7)
- added J84: 1x1, ao_tht:Perf_Board_Hole, F.Cu at (87.6, 62.2)
- added J85: 1x1, ao_tht:Perf_Board_Hole, F.Cu at (87.6, 64.8)
- added J86: 1x1, ao_tht:Perf_Board_Hole, F.Cu at (87.6, 67.3)
- added J87: 1x1, ao_tht:Perf_Board_Hole, F.Cu at (87.6, 69.8)
- added J88: 1x1, ao_tht:Perf_Board_Hole, F.Cu at (87.6, 72.4)
- added J89: 1x1, ao_tht:Perf_Board_Hole, F.Cu at (87.6, 74.9)
- added J9: 1x1, ao_tht:Perf_Board_Hole, F.Cu at (64.8, 77.5)
- added J90: 1x1, ao_tht:Perf_Board_Hole, F.Cu at (87.6, 77.5)
- added J91: 1x1, ao_tht:Perf_Board_Hole, F.Cu at (87.6, 80.0)
- added J92: 1x1, ao_tht:Perf_Board_Hole, F.Cu at (90.2, 59.7)
- added J93: 1x1, ao_tht:Perf_Board_Hole, F.Cu at (90.2, 62.2)
- added J94: 1x1, ao_tht:Perf_Board_Hole, F.Cu at (90.2, 64.8)
- added J95: 1x1, ao_tht:Perf_Board_Hole, F.Cu at (90.2, 67.3)
- added J96: 1x1, ao_tht:Perf_Board_Hole, F.Cu at (90.2, 69.8)
- added J97: 1x1, ao_tht:Perf_Board_Hole, F.Cu at (90.2, 72.4)
- added J98: 1x1, ao_tht:Perf_Board_Hole, F.Cu at (90.2, 74.9)
- added J99: 1x1, ao_tht:Perf_Board_Hole, F.Cu at (90.2, 77.5)
- J2, J3, J4, J5, J6, J7: value Conn_01x01 -> 1x1
- moved J2 40.6 mm to (64.8, 59.7)
- moved J4 33.0 mm to (64.8, 64.8)
- moved J6 33.0 mm to (64.8, 69.8)
- moved J7 12.7 mm to (64.8, 72.4)
- moved J5 2.54 mm to (64.8, 67.3)
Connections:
- J2 pad 1: +12V -> -12V
- J5 pad 1: GND -> Net-(J5-Pad1)
- J6 pad 1: -12V -> Net-(J5-Pad1)
- J7 pad 1: -12V -> Net-(J5-Pad1)
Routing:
- net GND: track 0.00 -> 195.6 mm
- net +12V: track 47.1 -> 199.5 mm
- net -12V: track 61.6 -> 208.9 mm
- net Net-(J281-Pad1): track 0.00 -> 76.2 mm
- net Net-(J10-Pad1): track 0.00 -> 76.2 mm
- net Net-(J95-Pad1): track 0.00 -> 10.2 mm
- net Net-(J86-Pad1): track 0.00 -> 10.2 mm
- net Net-(J77-Pad1): track 0.00 -> 10.2 mm
- net Net-(J68-Pad1): track 0.00 -> 10.2 mm
- net Net-(J59-Pad1): track 0.00 -> 10.2 mm
- net Net-(J552-Pad1): track 0.00 -> 10.2 mm
- net Net-(J543-Pad1): track 0.00 -> 10.2 mm
- net Net-(J534-Pad1): track 0.00 -> 10.2 mm
- net Net-(J525-Pad1): track 0.00 -> 10.2 mm
- net Net-(J516-Pad1): track 0.00 -> 10.2 mm
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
